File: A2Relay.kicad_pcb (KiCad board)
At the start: 2 copper layers, 33 x 30.5 mm, 7 parts, among them J1 Gameport, J2 Gamepad, J3 /RESET, J4 RELAY, U1 SN74ALS259, U2 SN74ALS259DR

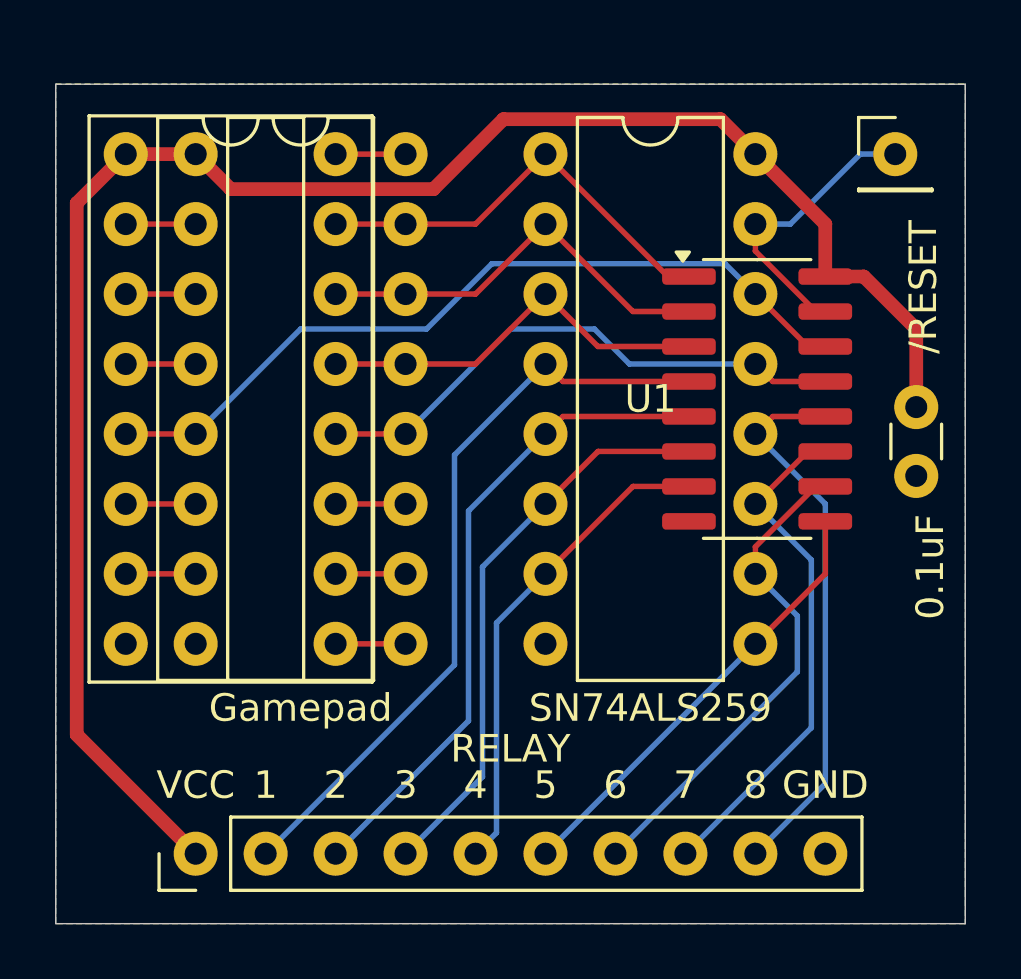
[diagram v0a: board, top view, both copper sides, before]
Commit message: Update to KiCad 9.0, add surface mount capacitor, swap VCC / GND on relay connector
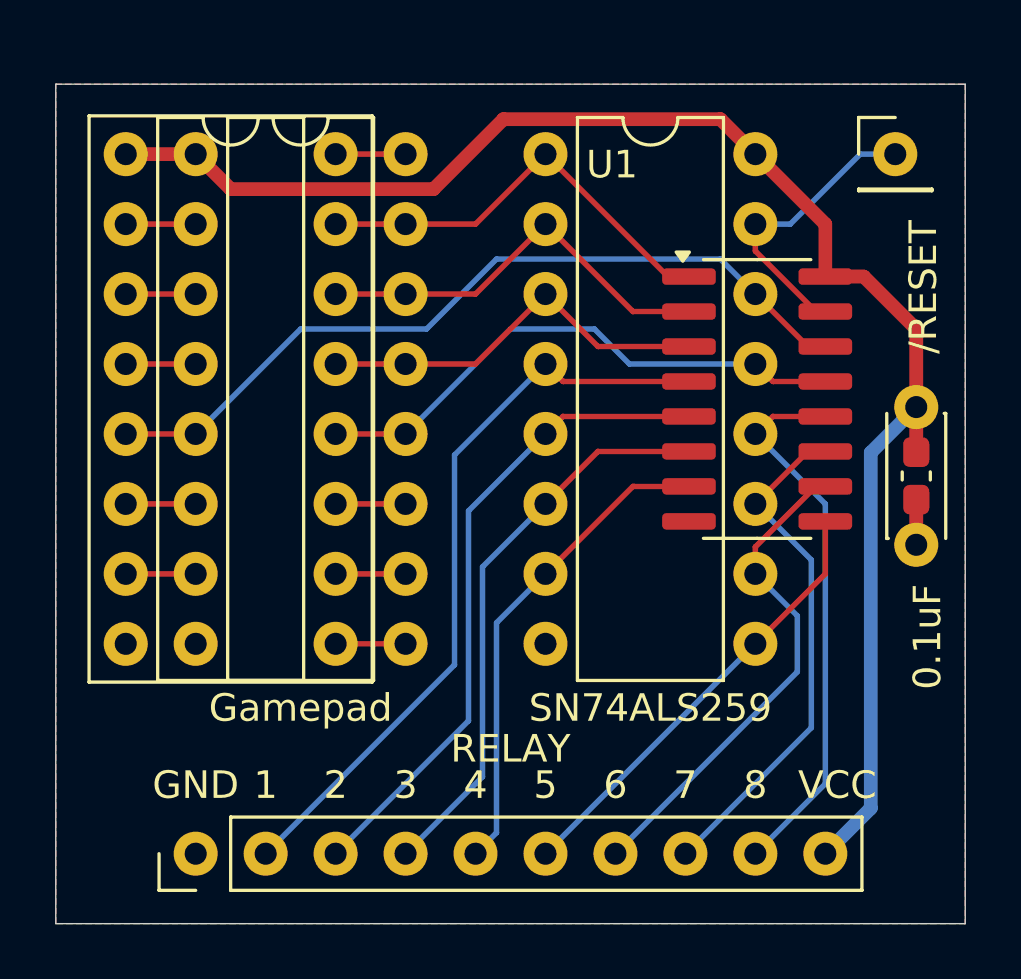
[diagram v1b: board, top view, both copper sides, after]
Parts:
- added C2: 0.1uF, Capacitor_SMD:C_0603_1608Metric_Pad1.08x0.95mm_HandSolder, F.Cu at (112.5, 57.4)
- C1: footprint Capacitor_THT:C_Disc_D3.0mm_W1.6mm_P2.50mm -> Capacitor_THT:C_Disc_D4.3mm_W1.9mm_P5.00mm
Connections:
- J4 pad 1: +5V -> GND
- J4 pad 10: GND -> +5V
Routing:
- net +5V: track 65.3 -> 56.6 mm
- net GND: track 0.00 -> 1.64 mm

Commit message: revision 3 - initial prototype run
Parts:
- added G***: LOGO, cityxen:deadline97, B.Cu at (102.0, 56.8)
- moved J3 0.90 mm to (111.1, 46.4)
- moved U1 0.90 mm to (98.4, 46.4)
- moved U2 0.90 mm to (106.1, 55.2)
- moved C1 0.81 mm to (112.0, 55.5)
- moved C2 0.81 mm to (112.0, 58.0)
- moved J1 0.63 mm to (83.8, 46.4)
- moved J2 0.63 mm to (86.4, 46.4)
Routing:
- net RESERVED: track 2.54 -> 0.00 mm
- net +5V: track 56.6 -> 54.4 mm
- net AN3: track 20.1 -> 18.5 mm
- net /STB: track 29.3 -> 27.7 mm
- net Q7: track 20.1 -> 19.1 mm
- net Q6: track 18.8 -> 17.8 mm
- net Q4: track 16.3 -> 15.4 mm
- net Q1: track 23.9 -> 23.0 mm
- net Q3: track 17.7 -> 16.8 mm
- net Q0: track 27.5 -> 26.6 mm
- net Q2: track 20.8 -> 19.9 mm
- net Q5: track 18.0 -> 17.1 mm
- net AN2: track 14.7 -> 14.0 mm
- net AN1: track 15.2 -> 14.6 mm
- net AN0: track 15.7 -> 15.1 mm
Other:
- board text added: "&"
- board text added: "Apple II Relay Board"
- board text added: "CityXen"
- board text added: "V2"
- board text added: "V2 Retro Computing"
- board text added: "by"
- board text added: "designed for"
- board text added: "revision 3 5-27-2026"
- board text added: "© 2026 David Kuder"
